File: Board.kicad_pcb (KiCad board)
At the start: 2 copper layers, 68 x 33 mm, 37 parts, among them J1 WAGO 2086-1202, J2 WAGO 2086-1202, J3 WAGO 2086-1230, J4 WAGO 2086-1230, SW1 TS-13P

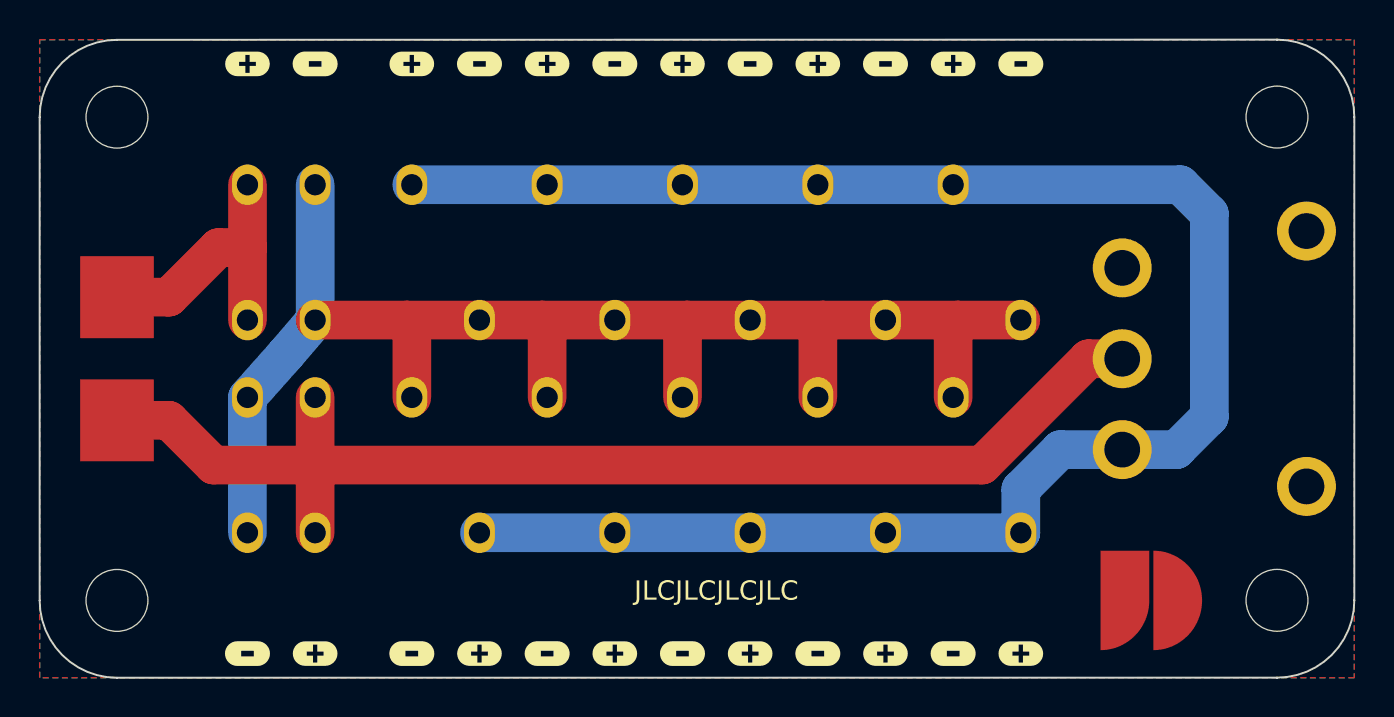
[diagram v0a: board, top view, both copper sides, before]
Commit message: update to KiCad 7
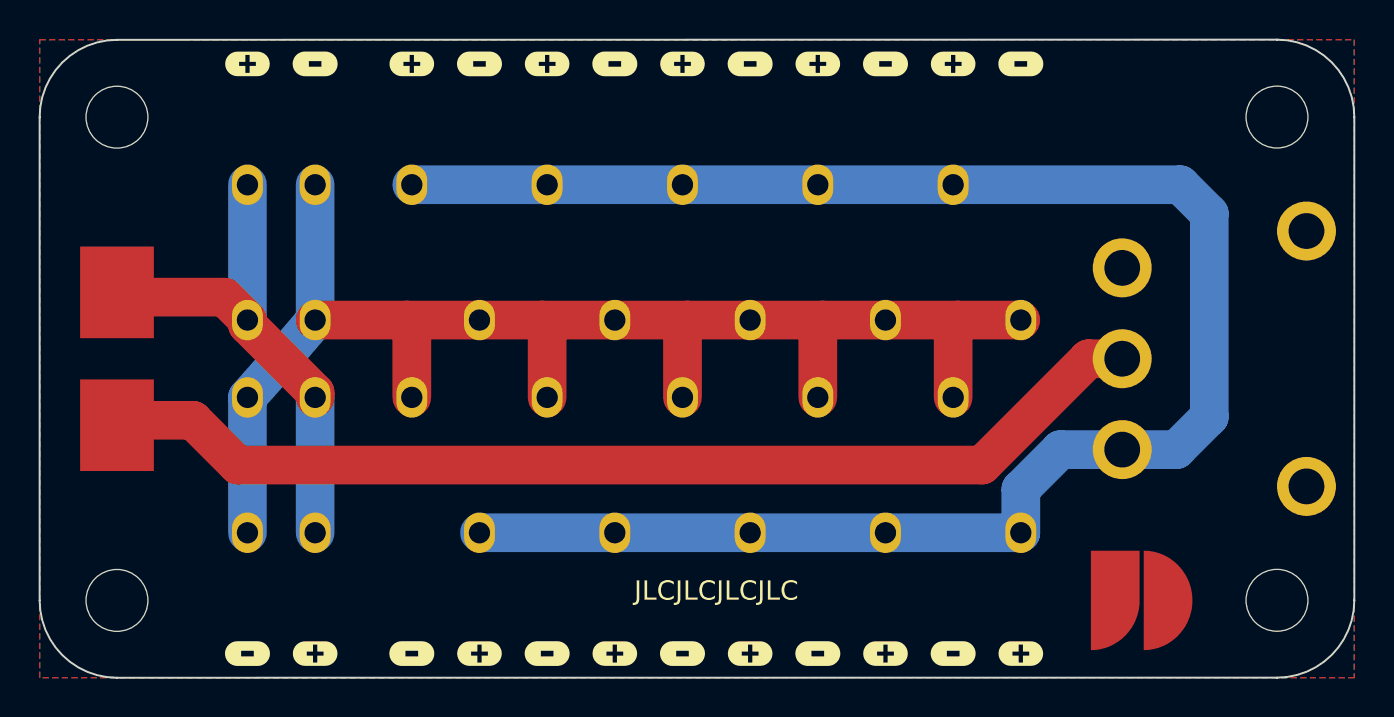
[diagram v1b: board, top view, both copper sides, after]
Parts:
- SW1: value TS-13P -> 500SSP1S1M6QEA
- moved REF** 0.50 mm to (161.0, 103.5)
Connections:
- F1 pad 1: Net-(F1-Pad1) -> PWR_P
- F1 pad 2: PWR_P -> Net-(SW1-Pad2)
- J1 pad 2: Net-(F1-Pad1) -> PWR_P
- SW1 pad 2: PWR_P -> Net-(SW1-Pad2)
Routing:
- net Net-(SW1-Pad2): track 0.00 -> 55.2 mm
- net PWR_P: track 62.2 -> 26.7 mm
- net Net-(F1-Pad1): track 14.8 -> 0.00 mm
